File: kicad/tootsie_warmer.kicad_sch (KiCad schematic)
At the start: 7 parts, among them SW1 SW_Add, SW2 SW_Stop, U1 WeMos_D1_mini

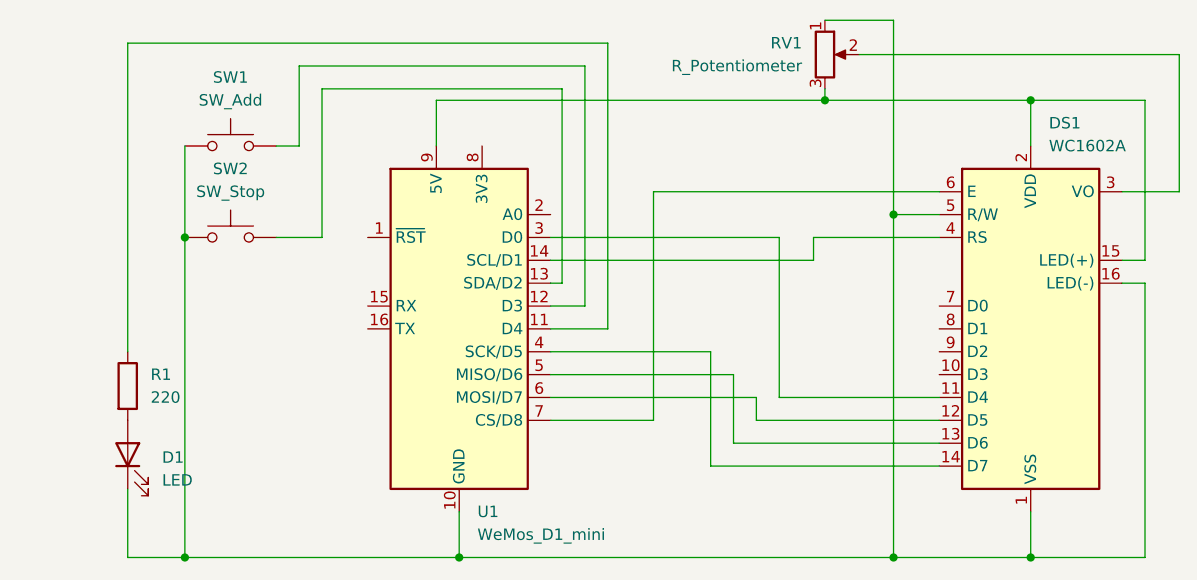
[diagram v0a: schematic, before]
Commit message: Update schema to have connector for relay
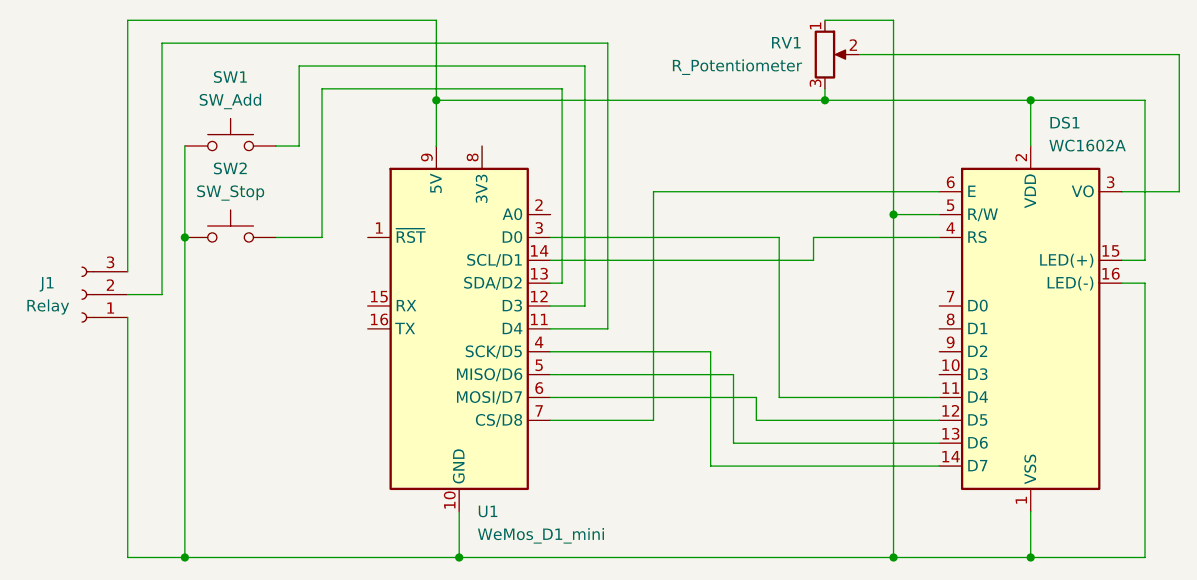
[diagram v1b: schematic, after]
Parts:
- removed D1: LED, LED_THT:LED_D4.0mm, symbol Device:LED
- removed R1: 220, Resistor_SMD:R_0201_0603Metric, symbol Device:R
- added J1: Relay, Connector_JST:JST_XH_B3B-XH-A_1x03_P2.50mm_Vertical, symbol Connector:Conn_01x03_Female
- RV1: footprint (none) -> Potentiometer_THT:Potentiometer_ACP_CA9-V10_Vertical
- SW1, SW2: footprint (none) -> Button_Switch_THT:SW_PUSH_6mm_H4.3mm
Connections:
- net at DS1.1 (VSS), DS1.16 (LED(-)), DS1.5 (R/W)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: now also J1.1 (Pin_1)
- net at U1.11 (D4): now also J1.2 (Pin_2)
- net at DS1.15 (LED(+)), DS1.2 (VDD), RV1.3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: now also J1.3 (Pin_3)
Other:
- title: (none) -> Tootsie Warmer
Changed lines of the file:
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@@
 (kicad_sch (version 20211123) (generator eeschema)
   (paper "A4")
+  (title_block
+    (title "Tootsie Warmer")
+    (date "2022-02-23")
+    (rev "v01")
+    (comment 3 "Apache License")
+    (comment 4 "Author: John Oxley")
+  )
   (junction (at 151.13 55.88) (diameter 0) (color 0 0 0 0)
   )
+  (junction (at 85.09 55.88) (diameter 0) (color 0 0 0 0)
+  )
   (junction (at 57.15 71.12) (diameter 0) (color 0 0 0 0)
   )
@@
     (stroke (width 0) (type default) (color 0 0 0 0))
   )
+  (wire (pts (xy 85.09 55.88) (xy 85.09 46.99))
+    (stroke (width 0) (type default) (color 0 0 0 0))
+  )
   (wire (pts (xy 120.65 91.44) (xy 120.65 88.9))
     (stroke (width 0) (type default) (color 0 0 0 0))
@@
     (stroke (width 0) (type default) (color 0 0 0 0))
   )
+  (wire (pts (xy 54.61 77.47) (xy 50.8 77.47))
+    (stroke (width 0) (type default) (color 0 0 0 0))
+  )
   (wire (pts (xy 101.6 52.07) (xy 101.6 78.74))
     (stroke (width 0) (type default) (color 0 0 0 0))
@@
     (stroke (width 0) (type default) (color 0 0 0 0))
   )
+  (wire (pts (xy 85.09 46.99) (xy 50.8 46.99))
+    (stroke (width 0) (type default) (color 0 0 0 0))
+  )
   (wire (pts (xy 50.8 106.68) (xy 57.15 106.68))
     (stroke (width 0) (type default) (color 0 0 0 0))
@@
     (stroke (width 0) (type default) (color 0 0 0 0))
   )
+  (wire (pts (xy 104.14 49.53) (xy 54.61 49.53))
+    (stroke (width 0) (type default) (color 0 0 0 0))
+  )
   (wire (pts (xy 140.97 88.9) (xy 123.19 88.9))
     (stroke (width 0) (type default) (color 0 0 0 0))
@@
     (stroke (width 0) (type default) (color 0 0 0 0))
   )
-  (wire (pts (xy 104.14 49.53) (xy 50.8 49.53))
-    (stroke (width 0) (type default) (color 0 0 0 0))
-  )
   (wire (pts (xy 151.13 55.88) (xy 128.27 55.88))
     (stroke (width 0) (type default) (color 0 0 0 0))
@@
     (stroke (width 0) (type default) (color 0 0 0 0))
   )
-  (wire (pts (xy 50.8 99.06) (xy 50.8 106.68))
+  (wire (pts (xy 50.8 80.01) (xy 50.8 106.68))
     (stroke (width 0) (type default) (color 0 0 0 0))
   )
@@
     (stroke (width 0) (type default) (color 0 0 0 0))
   )
+  (wire (pts (xy 50.8 46.99) (xy 50.8 74.93))
+    (stroke (width 0) (type default) (color 0 0 0 0))
+  )
+  (wire (pts (xy 54.61 49.53) (xy 54.61 77.47))
+    (stroke (width 0) (type default) (color 0 0 0 0))
+  )
   (wire (pts (xy 57.15 71.12) (xy 57.15 106.68))
     (stroke (width 0) (type default) (color 0 0 0 0))
@@
     (stroke (width 0) (type default) (color 0 0 0 0))
   )
-  (wire (pts (xy 50.8 49.53) (xy 50.8 83.82))
-    (stroke (width 0) (type default) (color 0 0 0 0))
-  )
   (wire (pts (xy 140.97 71.12) (xy 127 71.12))
     (stroke (width 0) (type default) (color 0 0 0 0))
@@
   (wire (pts (xy 118.11 86.36) (xy 97.79 86.36))
     (stroke (width 0) (type default) (color 0 0 0 0))
-  )
-  (symbol (lib_id "Device:LED") (at 50.8 95.25 90) (unit 1)
-    (in_bom yes) (on_board yes)
-    (property "Reference" "D1" (id 0) (at 54.61 95.5674 90)
-      (effects (font (size 1.27 1.27)) (justify right))
-    )
-    (property "Value" "LED" (id 1) (at 54.61 98.1074 90)
-      (effects (font (size 1.27 1.27)) (justify right))
-    )
-    (property "Footprint" "LED_THT:LED_D4.0mm" (id 2) (at 60.96 102.87 0)
-      (effects (font (size 1.27 1.27)) hide)
-    )
-    (property "Datasheet" "~" (id 3) (at 50.8 95.25 0)
-      (effects (font (size 1.27 1.27)) hide)
-    )
-    (pin "1")
-    (pin "2")
-  )
-  (symbol (lib_id "Device:R") (at 50.8 87.63 0) (unit 1)
-    (in_bom yes) (on_board yes) (fields_autoplaced)
-    (property "Reference" "R1" (id 0) (at 53.34 86.3599 0)
-      (effects (font (size 1.27 1.27)) (justify left))
-    )
-    (property "Value" "220" (id 1) (at 53.34 88.8999 0)
-      (effects (font (size 1.27 1.27)) (justify left))
-    )
-    (property "Footprint" "Resistor_SMD:R_0201_0603Metric" (id 2) (at 49.022 87.63 90)
-      (effects (font (size 1.27 1.27)) hide)
-    )
-    (property "Datasheet" "~" (id 3) (at 50.8 87.63 0)
-      (effects (font (size 1.27 1.27)) hide)
-    )
-    (pin "1")
-    (pin "2")
   )
   (symbol (lib_id "Display_Character:WC1602A") (at 151.13 81.28 0) (unit 1)
@@
     (property "Reference" "SW1" (id 0) (at 62.23 53.34 0))
     (property "Value" "SW_Add" (id 1) (at 62.23 55.88 0))
-    (property "Footprint" "" (id 2) (at 62.23 55.88 0)
+    (property "Footprint" "Button_Switch_THT:SW_PUSH_6mm_H4.3mm" (id 2) (at 62.23 55.88 0)
       (effects (font (size 1.27 1.27)) hide)
     )
@@
     (pin "1")
     (pin "2")
+  )
+  (symbol (lib_id "Connector:Conn_01x03_Female") (at 45.72 77.47 180) (unit 1)
+    (in_bom yes) (on_board yes)
+    (property "Reference" "J1" (id 0) (at 41.91 76.2 0))
+    (property "Value" "Relay" (id 1) (at 41.91 78.74 0))
+    (property "Footprint" "Connector_JST:JST_XH_B3B-XH-A_1x03_P2.50mm_Vertical" (id 2) (at 45.72 77.47 0)
+      (effects (font (size 1.27 1.27)) hide)
+    )
+    (property "Datasheet" "~" (id 3) (at 45.72 77.47 0)
+      (effects (font (size 1.27 1.27)) hide)
+    )
+    (pin "1")
+    (pin "2")
+    (pin "3")
   )
   (symbol (lib_id "Switch:SW_Push") (at 62.23 71.12 0) (unit 1)
@@
     (property "Reference" "SW2" (id 0) (at 62.23 63.5 0))
     (property "Value" "SW_Stop" (id 1) (at 62.23 66.04 0))
-    (property "Footprint" "" (id 2) (at 62.23 66.04 0)
+    (property "Footprint" "Button_Switch_THT:SW_PUSH_6mm_H4.3mm" (id 2) (at 62.23 66.04 0)
       (effects (font (size 1.27 1.27)) hide)
     )
@@
       (effects (font (size 1.27 1.27)) (justify right))
     )
-    (property "Footprint" "" (id 2) (at 128.27 50.8 0)
+    (property "Footprint" "Potentiometer_THT:Potentiometer_ACP_CA9-V10_Vertical" (id 2) (at 128.27 50.8 0)
       (effects (font (size 1.27 1.27)) hide)
     )
@@
   )
   (symbol_instances
-    (path "/1ad9d488-c5e8-4cde-8e90-084d46644ad2"
-      (reference "D1") (unit 1) (value "LED") (footprint "LED_THT:LED_D4.0mm")
-    )
     (path "/43aa9aec-4f6c-4be1-b6b6-092469141964"
       (reference "DS1") (unit 1) (value "WC1602A") (footprint "Display:WC1602A")
     )
-    (path "/21d8c47c-4cf0-4c07-9491-9a6bb6d4083a"
-      (reference "R1") (unit 1) (value "220") (footprint "Resistor_SMD:R_0201_0603Metric")
+    (path "/ae39d000-e1da-4f40-b995-9482be0f1de9"
+      (reference "J1") (unit 1) (value "Relay") (footprint "Connector_JST:JST_XH_B3B-XH-A_1x03_P2.50mm_Vertical")
     )
     (path "/d6b58f2b-a749-4f92-98d5-3e66c921649a"
-      (reference "RV1") (unit 1) (value "R_Potentiometer") (footprint "")
+      (reference "RV1") (unit 1) (value "R_Potentiometer") (footprint "Potentiometer_THT:Potentiometer_ACP_CA9-V10_Vertical")
     )
     (path "/aba14d70-9c4b-4774-9718-6bc4d86449a3"
-      (reference "SW1") (unit 1) (value "SW_Add") (footprint "")
+      (reference "SW1") (unit 1) (value "SW_Add") (footprint "Button_Switch_THT:SW_PUSH_6mm_H4.3mm")
     )
     (path "/cfe5df1e-d1f3-49cb-89ed-3fc7bab6345d"
-      (reference "SW2") (unit 1) (value "SW_Stop") (footprint "")
+      (reference "SW2") (unit 1) (value "SW_Stop") (footprint "Button_Switch_THT:SW_PUSH_6mm_H4.3mm")
     )
     (path "/71f8d568-0f23-4ff2-8e60-1600ce517a48"

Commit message: Swap D2 & D4.  Fixes #2
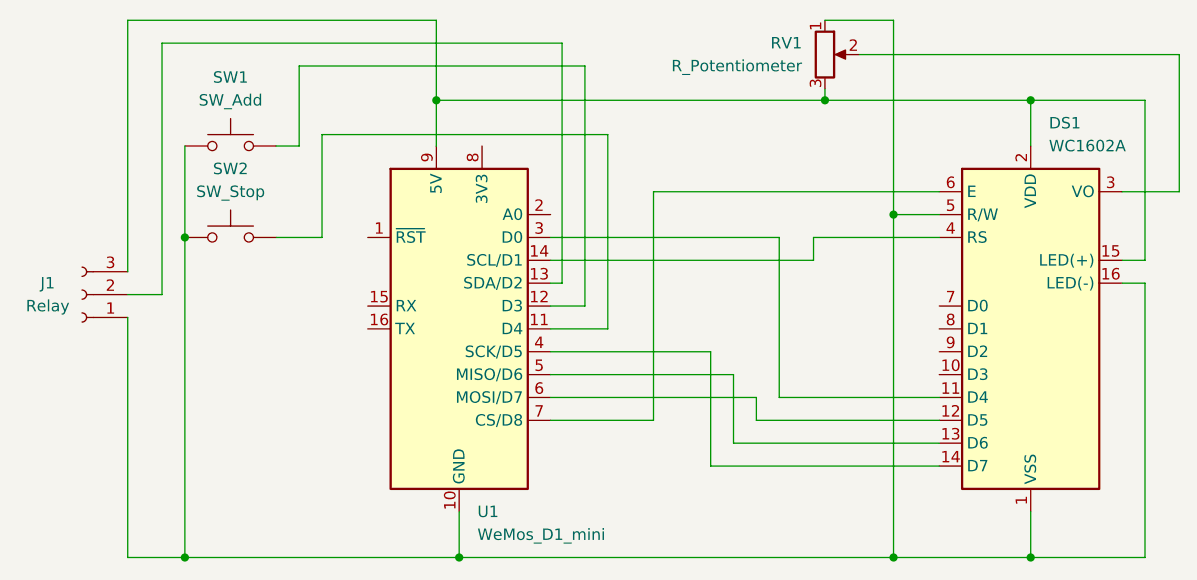
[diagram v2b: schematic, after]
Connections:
- net at U1.11 (D4): now also SW2.2; no longer J1.2 (Pin_2)
- net at U1.13 (SDA/D2): now also J1.2 (Pin_2); no longer SW2.2
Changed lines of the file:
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@@
-    (stroke (width 0) (type default) (color 0 0 0 0))
-  )
-  (wire (pts (xy 72.39 54.61) (xy 72.39 71.12))
     (stroke (width 0) (type default) (color 0 0 0 0))
   )
@@
   )
   (wire (pts (xy 85.09 55.88) (xy 85.09 46.99))
+    (stroke (width 0) (type default) (color 0 0 0 0))
+  )
+  (wire (pts (xy 104.14 59.69) (xy 104.14 81.28))
     (stroke (width 0) (type default) (color 0 0 0 0))
   )
@@
     (stroke (width 0) (type default) (color 0 0 0 0))
   )
-  (wire (pts (xy 104.14 49.53) (xy 54.61 49.53))
-    (stroke (width 0) (type default) (color 0 0 0 0))
-  )
   (wire (pts (xy 140.97 88.9) (xy 123.19 88.9))
     (stroke (width 0) (type default) (color 0 0 0 0))
@@
     (stroke (width 0) (type default) (color 0 0 0 0))
   )
-  (wire (pts (xy 72.39 71.12) (xy 67.31 71.12))
+  (wire (pts (xy 72.39 71.12) (xy 72.39 59.69))
     (stroke (width 0) (type default) (color 0 0 0 0))
   )
@@
     (stroke (width 0) (type default) (color 0 0 0 0))
   )
+  (wire (pts (xy 72.39 59.69) (xy 104.14 59.69))
+    (stroke (width 0) (type default) (color 0 0 0 0))
+  )
   (wire (pts (xy 50.8 46.99) (xy 50.8 74.93))
     (stroke (width 0) (type default) (color 0 0 0 0))
@@
   )
   (wire (pts (xy 57.15 71.12) (xy 57.15 106.68))
-    (stroke (width 0) (type default) (color 0 0 0 0))
-  )
-  (wire (pts (xy 99.06 54.61) (xy 72.39 54.61))
     (stroke (width 0) (type default) (color 0 0 0 0))
   )
@@
     (stroke (width 0) (type default) (color 0 0 0 0))
   )
+  (wire (pts (xy 99.06 49.53) (xy 54.61 49.53))
+    (stroke (width 0) (type default) (color 0 0 0 0))
+  )
   (wire (pts (xy 69.85 60.96) (xy 67.31 60.96))
     (stroke (width 0) (type default) (color 0 0 0 0))
@@
     (stroke (width 0) (type default) (color 0 0 0 0))
   )
-  (wire (pts (xy 99.06 54.61) (xy 99.06 76.2))
+  (wire (pts (xy 99.06 49.53) (xy 99.06 76.2))
     (stroke (width 0) (type default) (color 0 0 0 0))
   )
@@
     (stroke (width 0) (type default) (color 0 0 0 0))
   )
-  (wire (pts (xy 104.14 49.53) (xy 104.14 81.28))
+  (wire (pts (xy 67.31 71.12) (xy 72.39 71.12))
     (stroke (width 0) (type default) (color 0 0 0 0))
   )
